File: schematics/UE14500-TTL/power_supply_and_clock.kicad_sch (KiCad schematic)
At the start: 8 parts, among them J3 5VDC IN, SW1 Power On, SW2 Reset

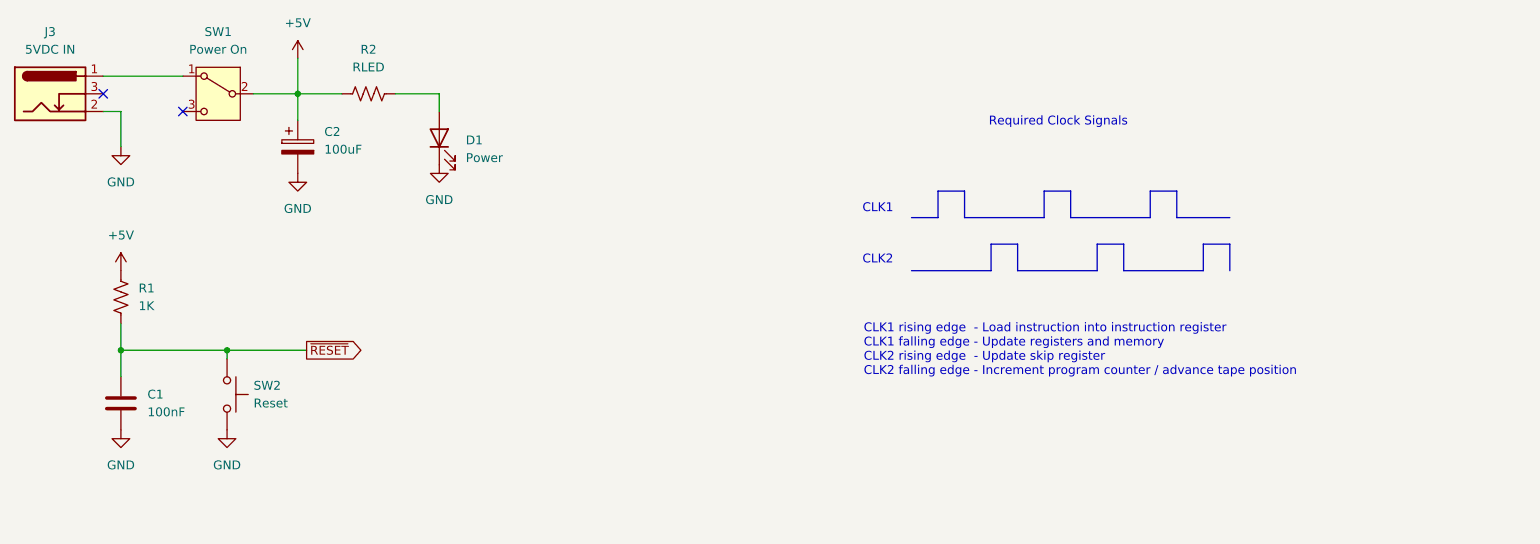
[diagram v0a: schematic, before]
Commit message: Add a tape "REWIND" opcode to reset the PC early
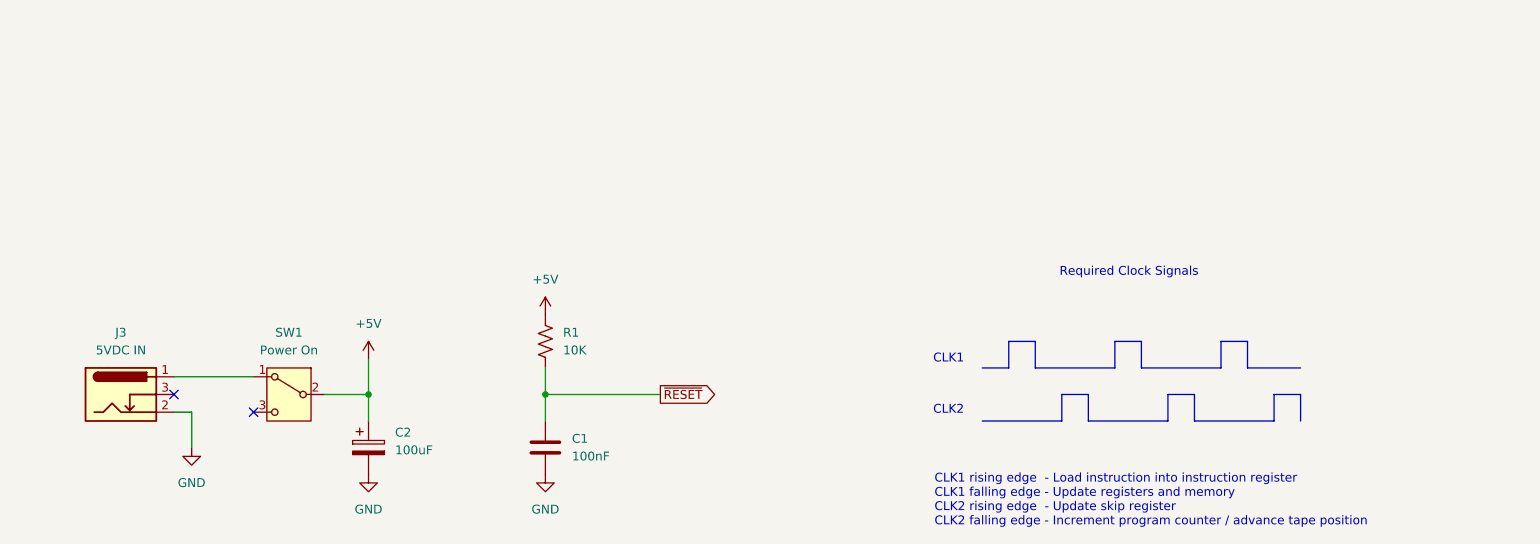
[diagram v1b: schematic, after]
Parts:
- removed D1: Power, LED_THT:LED_D3.0mm, symbol Device:LED
- removed R2: RLED, Resistor_THT:R_Axial_DIN0207_L6.3mm_D2.5mm_P10.16mm_Horizontal, symbol Device:R_US
- removed SW2: Reset, Button_Switch_THT:SW_PUSH_6mm, symbol Switch:SW_Push
- R1: value 1K -> 10K
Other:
- moved on the sheet: C1, C2, J3, R1, SW1

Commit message: Make some renderings of the computer
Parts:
- renumbered C2 to C1, C1 to C2
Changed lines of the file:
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@@
 		(dnp no)
 		(fields_autoplaced yes)
-		(property "Reference" "#PWR13"
+		(property "Reference" "#PWR10"
 			(at 91.44 96.52 0)
 			(effects
@@
 			(project "UE14500-TTL"
 				(path "/3387ba40-0694-43b2-a156-d12ce9552f1f/6f92b49c-fbab-43f8-8bb9-366de87fd5f1"
-					(reference "#PWR13")
+					(reference "#PWR10")
 					(unit 1)
 				)
@@
 		(dnp no)
 		(fields_autoplaced yes)
-		(property "Reference" "#PWR11"
+		(property "Reference" "#PWR13"
 			(at 116.84 115.57 0)
 			(effects
@@
 			(project "UE14500-TTL"
 				(path "/3387ba40-0694-43b2-a156-d12ce9552f1f/6f92b49c-fbab-43f8-8bb9-366de87fd5f1"
-					(reference "#PWR11")
+					(reference "#PWR13")
 					(unit 1)
 				)
@@
 		(dnp no)
 		(fields_autoplaced yes)
-		(property "Reference" "C2"
+		(property "Reference" "C1"
 			(at 95.25 103.2509 0)
 			(effects
@@
 			(project ""
 				(path "/3387ba40-0694-43b2-a156-d12ce9552f1f/6f92b49c-fbab-43f8-8bb9-366de87fd5f1"
-					(reference "C2")
+					(reference "C1")
 					(unit 1)
 				)
@@
 		(dnp no)
 		(fields_autoplaced yes)
-		(property "Reference" "#PWR10"
+		(property "Reference" "#PWR12"
 			(at 116.84 90.17 0)
 			(effects
@@
 			(project "UE14500-TTL"
 				(path "/3387ba40-0694-43b2-a156-d12ce9552f1f/6f92b49c-fbab-43f8-8bb9-366de87fd5f1"
-					(reference "#PWR10")
+					(reference "#PWR12")
 					(unit 1)
 				)
@@
 		(dnp no)
 		(fields_autoplaced yes)
-		(property "Reference" "C1"
+		(property "Reference" "C2"
 			(at 120.65 104.1399 0)
 			(effects
@@
 			(project ""
 				(path "/3387ba40-0694-43b2-a156-d12ce9552f1f/6f92b49c-fbab-43f8-8bb9-366de87fd5f1"
-					(reference "C1")
+					(reference "C2")
 					(unit 1)
 				)
@@
 		(dnp no)
 		(fields_autoplaced yes)
-		(property "Reference" "#PWR14"
+		(property "Reference" "#PWR11"
 			(at 91.44 115.57 0)
 			(effects
@@
 			(project "UE14500-TTL"
 				(path "/3387ba40-0694-43b2-a156-d12ce9552f1f/6f92b49c-fbab-43f8-8bb9-366de87fd5f1"
-					(reference "#PWR14")
-					(unit 1)
-				)
+					(reference "#PWR11")
+					(unit 1)
+				)

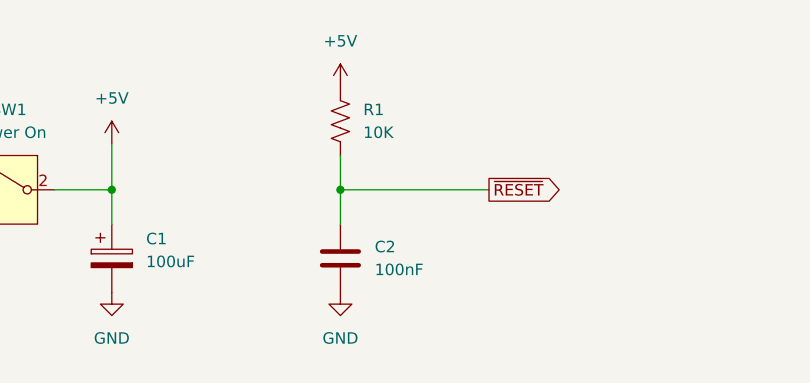
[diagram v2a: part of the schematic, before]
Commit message: Change capacitor in reset RC circuit to 1uF
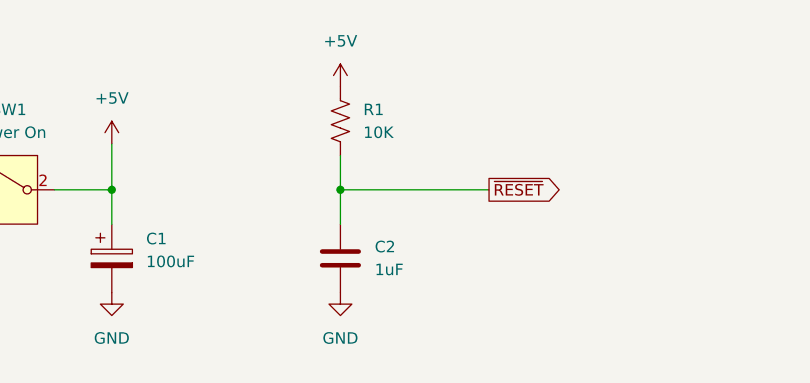
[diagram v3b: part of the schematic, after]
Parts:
- C2: value 100nF -> 1uF
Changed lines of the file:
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@@
 			)
 		)
-		(property "Value" "100nF"
+		(property "Value" "1uF"
 			(at 120.65 106.6799 0)
 			(effects
